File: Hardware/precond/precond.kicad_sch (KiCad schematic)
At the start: 37 parts, among them J1 Conn_Coaxial, J2 Conn_Coaxial, J3 Buck_logic_in, J4 3.3V_header, J5 XADC_headder, Q1 IRLML6344TRPBF, Q2 IRLML9301TRPBF, U1 OPA2340, U2 OPA2340

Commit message: bug fix
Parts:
- R5: value 1k -> 100
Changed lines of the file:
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@@
 			)
 		)
-		(property "Value" "1k"
-			(at 142.748 129.286 0)
+		(property "Value" "100"
+			(at 142.24 129.286 0)
 			(effects
 				(font

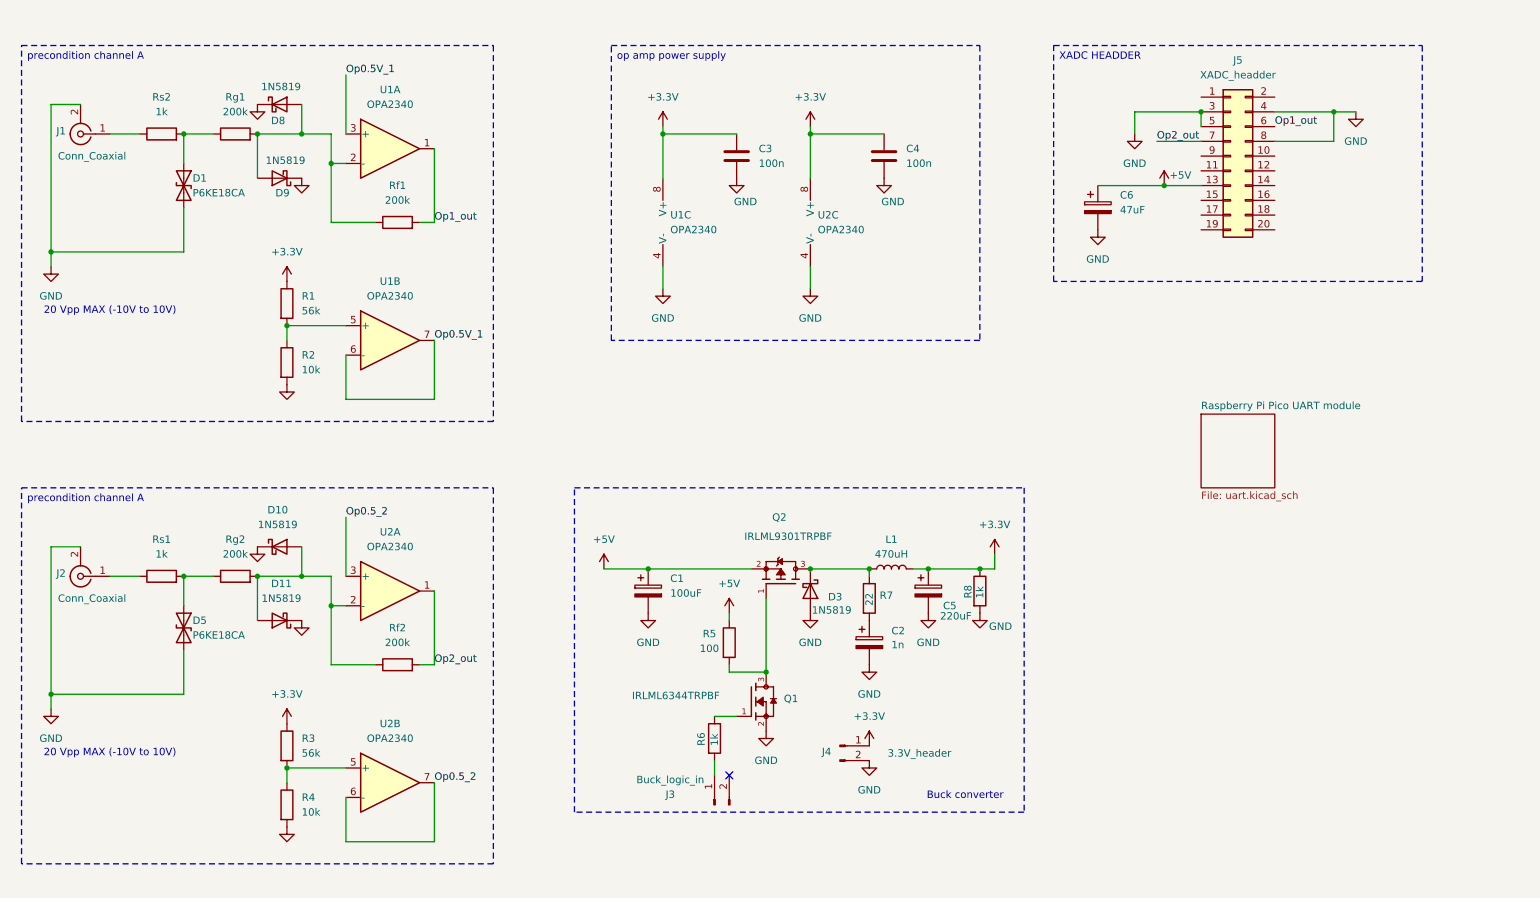
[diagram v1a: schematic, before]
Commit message: PCB schematic changes
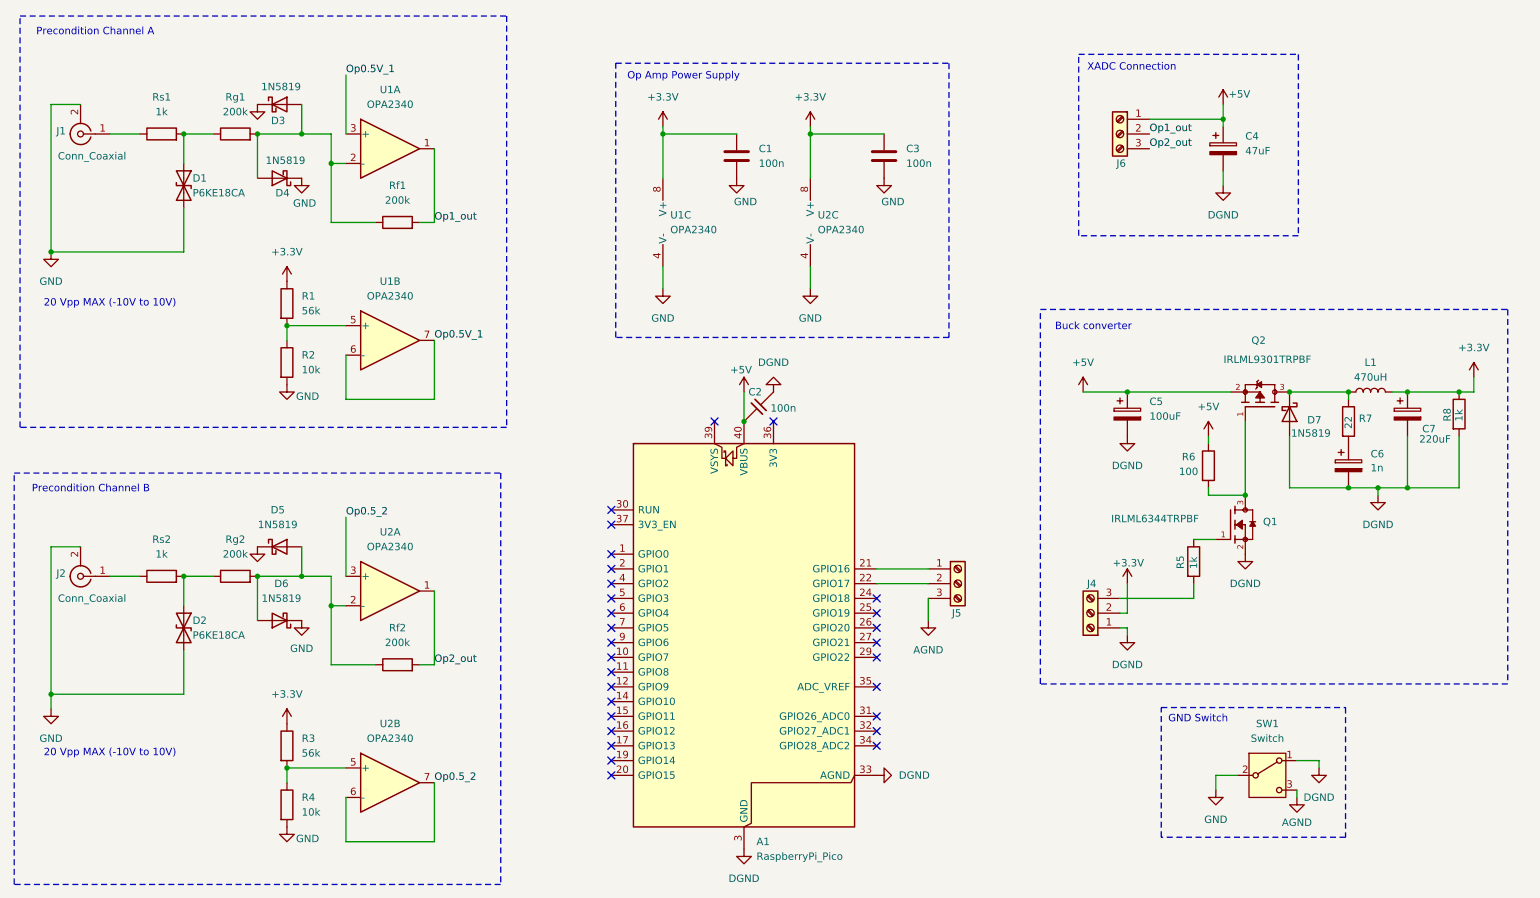
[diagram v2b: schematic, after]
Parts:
- removed J3: Buck_logic_in, Connector_JST:JST_PH_B2B-PH-K_1x02_P2.00mm_Vertical, symbol Connector:Conn_01x02_Pin
- removed J4: 3.3V_header, Connector_JST:JST_PH_B2B-PH-K_1x02_P2.00mm_Vertical, symbol Connector:Conn_01x02_Pin
- removed J5: XADC_headder, Connector_PinSocket_2.00mm:PinSocket_2x10_P2.00mm_Vertical, symbol Connector_Generic:Conn_02x10_Odd_Even
- added A1: RaspberryPi_Pico, Module:RaspberryPi_Pico_Common_THT, symbol MCU_Module:RaspberryPi_Pico
- added C2: 100n, Capacitor_THT:C_Rect_L7.2mm_W2.5mm_P5.00mm_FKS2_FKP2_MKS2_MKP2, symbol Device:C_45deg
- added J4, J5, J6: Screw_Terminal_01x03, Connector_PinHeader_2.54mm:PinHeader_1x03_P2.54mm_Vertical, symbol Connector:Screw_Terminal_01x03
- added SW1: Switch, symbol Switch:SW_SPDT
- renumbered C3 to C1, C4 to C3, C6 to C4, C1 to C5, C2 to C6, C5 to C7, D5 to D2, D8 to D3, D9 to D4, D10 to D5, D11 to D6, D3 to D7, R6 to R5, R5 to R6, Rs2 to Rs1, Rs1 to Rs2
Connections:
- net +3.3V: now also J4.2 (Pin_2)
- net +5V: now also A1.40 (VBUS), C2.2, J6.1 (Pin_1)
- net GND: now also SW1.2 (B); no longer C4.2, C5.2, C6.2, C7.2, D7.2 (A), Q1.2, R8.2
- net Op1_out: now also J6.2 (Pin_2)
- net Op2_out: now also J6.3 (Pin_3)
- net at R5.2: now also J4.3 (Pin_3)
- new net: A1.21 (GPIO16), J5.1 (Pin_1)
- new net: A1.22 (GPIO17), J5.2 (Pin_2)
- new net AGND: J5.3 (Pin_3), SW1.3 (C)
- new net DGND: A1.13 (GND), A1.18 (GND), A1.23 (GND), A1.28 (GND), A1.3 (GND), A1.33 (AGND), A1.38 (GND), A1.8 (GND), C2.1, C4.2, C5.2, C6.2, C7.2, D7.2 (A), J4.1 (Pin_1), Q1.2, R8.2, SW1.1 (A)
- no-connect marks 1 -> 29
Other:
- removed sheet Raspberry Pi Pico UART module
- note added: "GND Switch"
- note added: "Op Amp Power Supply"
- note added: "Precondition Channel A"
- note added: "Precondition Channel B"
- note added: "XADC Connection"
- moved on the sheet: C4, C5, C6, C7, D7, L1, Q1, Q2, R5, R6, R7, R8

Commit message: yanis do the thing you wanted i left the header and microcontroller for you on top
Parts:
- added TP1, TP2, TP3, TP4, TP5: TestPoint, symbol Connector:TestPoint
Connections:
- net +3.3V: now also TP1.1
- net Op1_out: now also TP2.1
- net Op2_out: now also TP3.1
- net at J1.1 (In), Rs1.1: now also TP5.1
- net at J2.1 (In), Rs2.1: now also TP4.1

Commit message: no
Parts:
- removed J5, J6: Screw_Terminal_01x03, Connector_PinHeader_2.54mm:PinHeader_1x03_P2.54mm_Vertical, symbol Connector:Screw_Terminal_01x03
- removed SW1: Switch, symbol Switch:SW_SPDT
- added C8, C9: 100n, Capacitor_THT:C_Rect_L7.2mm_W2.5mm_P5.00mm_FKS2_FKP2_MKS2_MKP2, symbol Device:C
- added H1: MountingHole, MountingHole:MountingHole_3.2mm_M3, symbol Mechanical:MountingHole
- added J3: XADC_header, Connector_PinSocket_2.00mm:PinSocket_2x10_P2.00mm_Vertical, symbol Connector_Generic:Conn_02x10_Odd_Even
- added J5: UART_hdr, Connector_JST:JST_PH_B3B-PH-K_1x03_P2.00mm_Vertical, symbol Connector:Conn_01x03_Pin
- J4: footprint Connector_PinHeader_2.54mm:PinHeader_1x03_P2.54mm_Vertical -> TerminalBlock_MetzConnect:TerminalBlock_MetzConnect_Type011_RT05503HBLC_1x03_P5.00mm_Horizontal
- R7: footprint Resistor_SMD:R_0805_2012Metric -> Resistor_SMD:R_2512_6332Metric
- TP1, TP2, TP3, TP4, TP5: footprint (none) -> TestPoint:TestPoint_Pad_2.5x2.5mm
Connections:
- net DGND is gone; now on net AGND: A1.13 (GND), A1.18 (GND), A1.23 (GND), A1.28 (GND), A1.3 (GND), A1.33 (AGND), A1.38 (GND), A1.8 (GND), C2.1, C4.2, C5.2, C6.2, C7.2, D7.2 (A), J4.1 (Pin_1), Q1.2, R8.2
- net +3.3V: now also D4.1 (K), D6.1 (K)
- net +5V: now also J3.13 (Pin_13)
- net AGND: now also C1.2, C3.2, D1.2 (A2), D2.2 (A2), D3.2 (A), D5.1 (K), J1.2 (Ext), J2.2 (Ext), R2.2, R4.2, U1.4 (V-), U2.4 (V-), C8.2, C9.2, J3.1 (Pin_1), J3.10 (Pin_10), J3.3 (Pin_3), J3.4 (Pin_4), J3.5 (Pin_5), J3.8 (Pin_8), J5.1 (Pin_1)
- net Op0.5V_1: now also C9.1
- net Op0.5_2: now also C8.1
- net Op1_out: now also J3.2 (Pin_2), J3.6 (Pin_6)
- net Op2_out: now also J3.7 (Pin_7)
- net at D4.2 (A), Rf1.1, Rg1.2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: now also D3.1 (K); no longer D3.2 (A)
- net at A1.21 (GPIO16): now also J5.3 (Pin_3)
- net at A1.22 (GPIO17): now also J5.2 (Pin_2)
- removed net GND: C1.2, C3.2, D1.2 (A2), D2.2 (A2), D3.1 (K), D4.1 (K), D5.1 (K), D6.1 (K), J1.2 (Ext), J2.2 (Ext), R2.2, R4.2, U1.4 (V-), U2.4 (V-)
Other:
- note added: "Pi Pico UART"
- note removed: "GND Switch"
- note removed: "XADC Connection"
- moved on the sheet: A1, C1, C2, C3, D3, TP1, U1C, U2C

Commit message: finished?
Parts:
- J5: footprint Connector_JST:JST_PH_B3B-PH-K_1x03_P2.00mm_Vertical -> Connector_PinHeader_2.54mm:PinHeader_1x03_P2.54mm_Vertical
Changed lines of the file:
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@@
 			)
 		)
-		(property "Footprint" "Connector_JST:JST_PH_B3B-PH-K_1x03_P2.00mm_Vertical"
+		(property "Footprint" "Connector_PinHeader_2.54mm:PinHeader_1x03_P2.54mm_Vertical"
 			(at 179.07 111.76 0)
 			(effects
